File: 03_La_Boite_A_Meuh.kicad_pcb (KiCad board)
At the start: 2 copper layers, 100 x 100 mm, 63 parts, among them J1 Micro_SD_Card, J10 Conn_01x01, J11 Conn_01x04, J18 Conn_01x02, J2 Conn_01x06, J26 Conn_01x02, J29 Conn_01x02, J3 Conn_01x08, J4 Conn_01x02, J5 Conn_02x02_Counter_Clockwise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

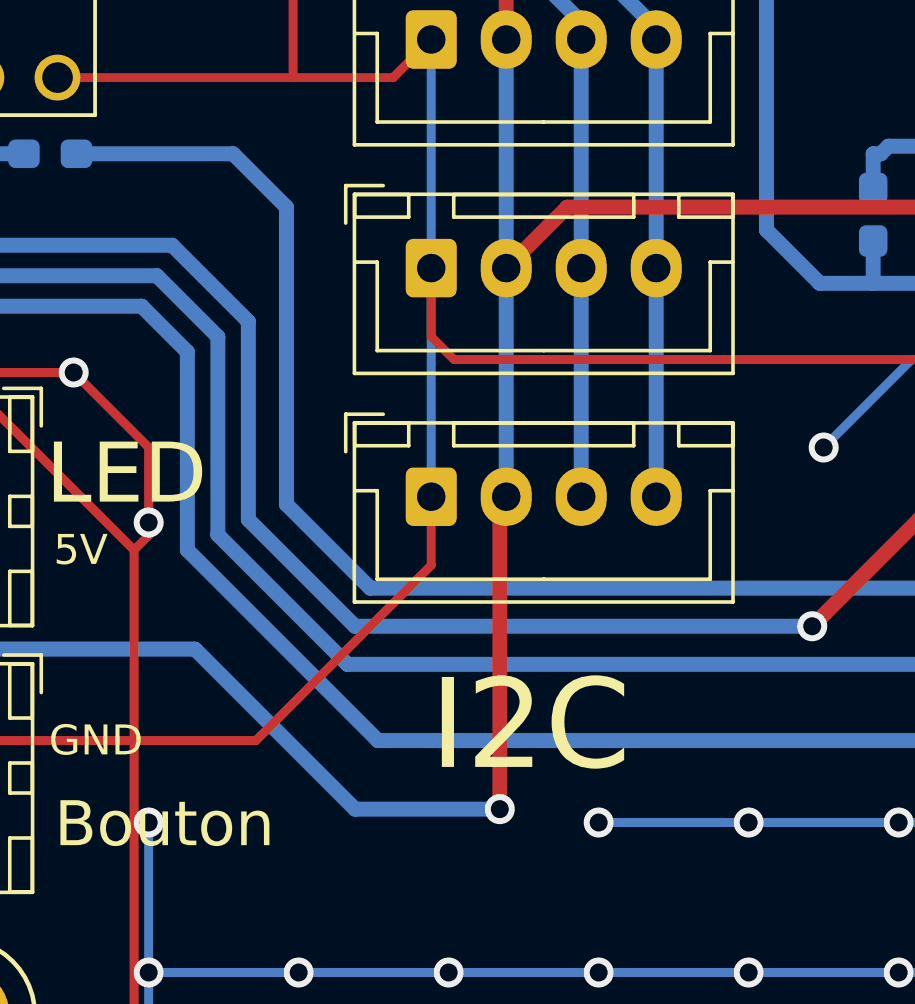
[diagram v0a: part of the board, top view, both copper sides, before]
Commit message: ajout strap sur dernier connecteur I2C
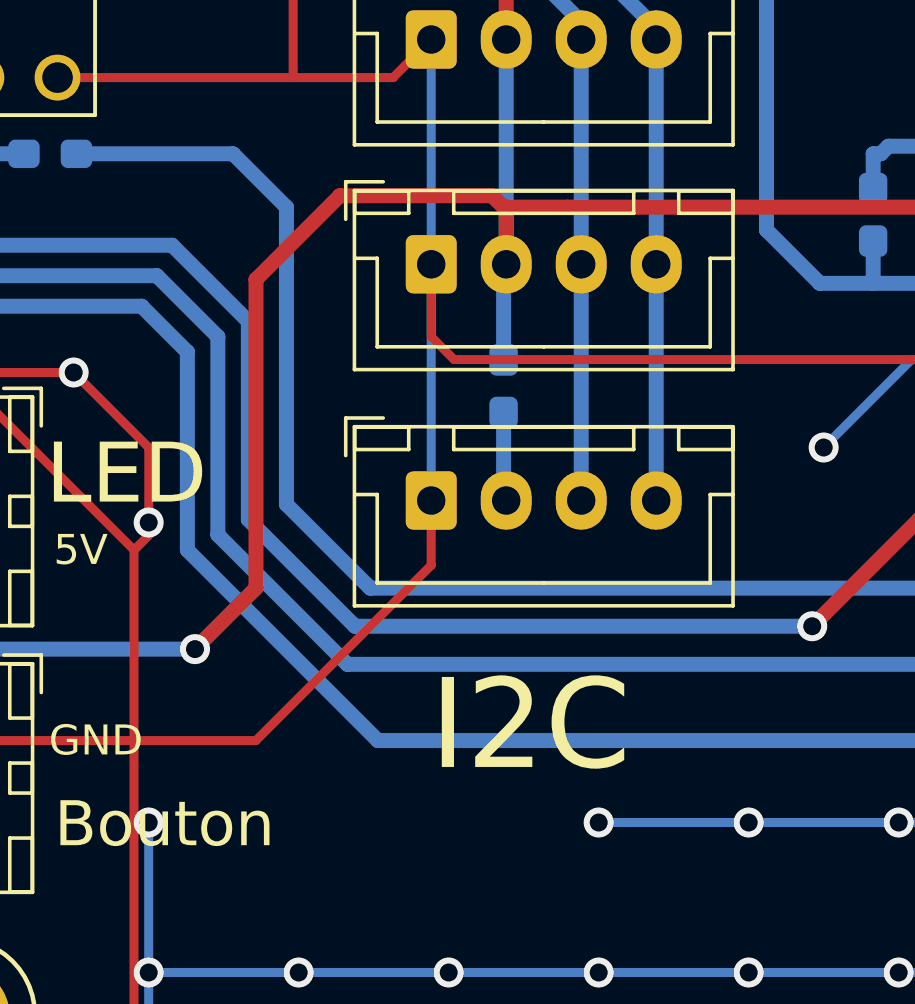
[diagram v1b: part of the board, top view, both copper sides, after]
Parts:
- added R21: 0, Resistor_SMD:R_0603_1608Metric_Pad1.05x0.95mm_HandSolder, B.Cu at (171.8, 100.5)
- moved J11 7.75 mm to (169.4, 104.3)
- moved J8 7.75 mm to (169.4, 96.4)
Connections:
- J11 pad 2: 3V3 -> Net-(J11-Pad2)
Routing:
- net 3V3: track 186.9 -> 183.5 mm
- net Net-(J11-Pad2): track 0.00 -> 3.27 mm

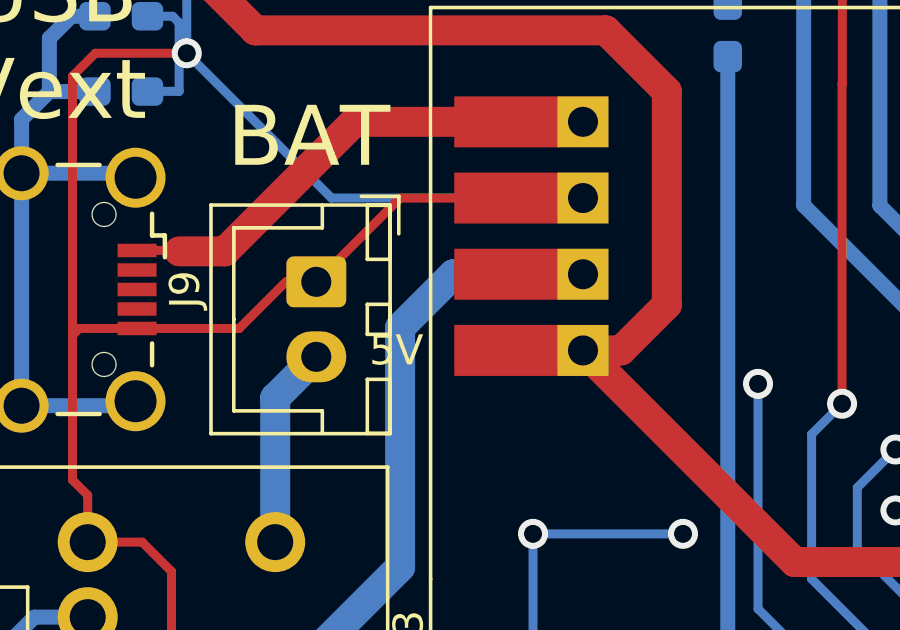
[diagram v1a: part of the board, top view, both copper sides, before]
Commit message: chgt connecteur batterie
connecteur batterie JST XH changé pour un PH + inversion des fils. schéma + routage fait
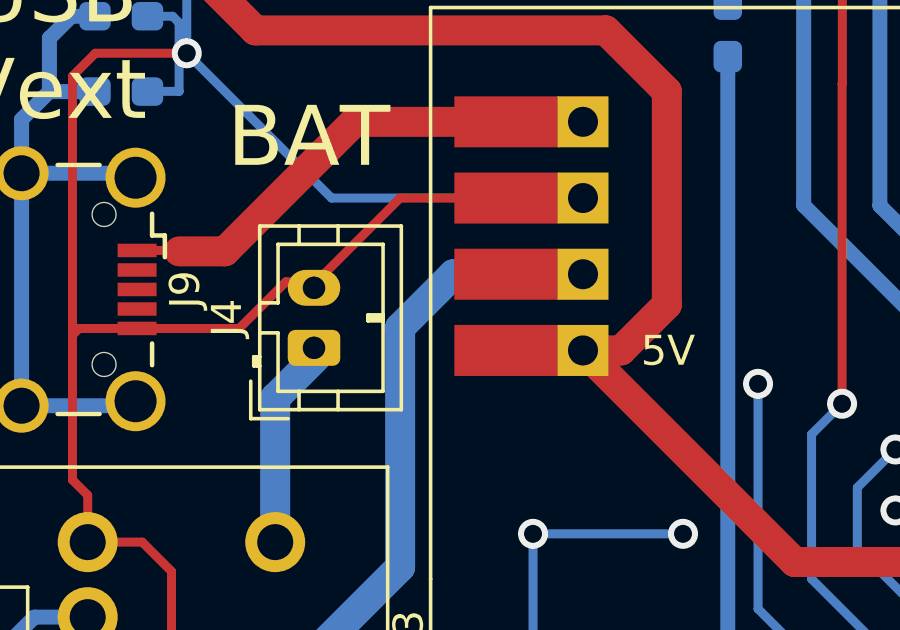
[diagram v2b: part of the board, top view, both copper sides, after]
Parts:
- J4: footprint Connector_JST:JST_XH_B2B-XH-A_1x02_P2.50mm_Vertical -> Connector_JST:JST_PH_B2B-PH-K_1x02_P2.00mm_Vertical
- moved J4 2.20 mm to (112.7, 103.8), turned to 90 degrees
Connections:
- J4 pad 1: GND -> VBAT1
- J4 pad 2: VBAT1 -> GND

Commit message: maj split librairie
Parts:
- U1: footprint Chimere:Audio_Facile -> Chimere_mods:Audio_Facile
- U2: footprint Chimere:MODULE_ESP32-DEVKITC -> Chimere_comps:MODULE_ESP32-DEVKITC
- U3: footprint Chimere:PTR901 -> Chimere_comps:PTR901
- U4: footprint Chimere:Batt_Alim -> Chimere_mods:Batt_Alim
- U5: footprint Chimere:Adafruit_UDA1334 -> Chimere_comps:Adafruit_UDA1334

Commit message: passage à la version "HP" de audio facile
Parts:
- U1: footprint Chimere_mods:Audio_Facile -> Chimere_mods:Audio_Facile_HP

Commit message: Changement pour Batt_alim_4P version _HP
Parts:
- U4: footprint Chimere_mods:Batt_Alim -> Chimere_mods:Batt_Alim_4P_HP
